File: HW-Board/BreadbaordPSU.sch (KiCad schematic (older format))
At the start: 12 parts

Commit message: sync
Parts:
- added C2, C4: 2.2u, symbol Device:C_Small
- added C3: 1u, symbol Device:C_Small
- added J2: Outputs, symbol Connector:Screw_Terminal_01x03
- added R2: 0r, symbol Device:R
- added U1: MAX6241, Housings_SOIC:SOIC-8_3.9x4.9mm_Pitch1.27mm, symbol Peters:MAX6241
- gave numbers to parts that had none: 12
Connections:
- net labels added: +4.096Vref, GNDA
- wire segments 25 -> 49
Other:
- note added: "Banana binding posts"
- note added: "Mind noise in layout"

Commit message: sync
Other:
- note added: "Todo:\n\nMerge to fewer opamps\nex. OPA2189IDR"
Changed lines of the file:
@@
 Text Notes 8500 5100 0    50   ~ 0
 Banana binding posts
+Text Notes 1400 6500 0    50   ~ 0
+Todo:\n\nMerge to fewer opamps\nex. OPA2189IDR
 $EndSCHEMATC

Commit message: SYNC
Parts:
- D1: value D_Zener -> 10V
- Q1: symbol Peters:Si4435 -> BreadbaordPSU-rescue:Si4435-Peters
- R1: value R -> 100k
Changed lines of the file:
@@
 	4150 1550 4250 1550
 $Comp
-L Peters:Si4435 Q1
+L BreadbaordPSU-rescue:Si4435-Peters Q1
 U 1 1 5CF021A1
 P 2300 1350
@@
 P 2650 1400
 F 0 "D1" V 2604 1479 50  0000 L CNN
-F 1 "D_Zener" V 2695 1479 50  0000 L CNN
+F 1 "10V" V 2695 1479 50  0000 L CNN
 F 2 "" H 2650 1400 50  0001 C CNN
 F 3 "~" H 2650 1400 50  0001 C CNN
@@
 P 2300 1700
 F 0 "R1" H 2370 1746 50  0000 L CNN
-F 1 "R" H 2370 1655 50  0000 L CNN
+F 1 "100k" H 2370 1655 50  0000 L CNN
 F 2 "" V 2230 1700 50  0001 C CNN
 F 3 "~" H 2300 1700 50  0001 C CNN

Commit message: sync
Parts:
- C1: value CP -> 100u
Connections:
- net at D1.1 (K), F1.1, Q1.1 (S): no longer Q1.2 (S), Q1.3 (S)
- net at C1.1, J1.2 (Pin_2), Q1.5 (D): no longer Q1.6 (D), Q1.7 (D), Q1.8 (D)
- new net: Q1.2 (S), Q1.3 (S)
- new net: Q1.6 (D), Q1.7 (D), Q1.8 (D)
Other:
- note added: "Max 15V"
- moved on the sheet: C1, D1, J1, Q1, R1
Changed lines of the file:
@@
 L Connector:Screw_Terminal_01x02 J1
 U 1 1 5CF83871
-P 1450 1350
-F 0 "J1" H 1368 1025 50  0000 C CNN
-F 1 "vin" H 1368 1116 50  0000 C CNN
-F 2 "" H 1450 1350 50  0001 C CNN
-F 3 "~" H 1450 1350 50  0001 C CNN
-	1    1450 1350
+P 1100 1350
+F 0 "J1" H 1018 1025 50  0000 C CNN
+F 1 "vin" H 1018 1116 50  0000 C CNN
+F 2 "" H 1100 1350 50  0001 C CNN
+F 3 "~" H 1100 1350 50  0001 C CNN
+	1    1100 1350
 	-1   0    0    1
 $EndComp
@@
 L power:GNDPWR #PWR0105
 U 1 1 5CF84A70
-P 1650 1400
-F 0 "#PWR0105" H 1650 1200 50  0001 C CNN
-F 1 "GNDPWR" H 1654 1246 50  0000 C CNN
-F 2 "" H 1650 1350 50  0001 C CNN
-F 3 "" H 1650 1350 50  0001 C CNN
-	1    1650 1400
-	1    0    0    -1
-$EndComp
-Wire Wire Line
-	1650 1350 1650 1400
+P 1300 1400
+F 0 "#PWR0105" H 1300 1200 50  0001 C CNN
+F 1 "GNDPWR" H 1304 1246 50  0000 C CNN
+F 2 "" H 1300 1350 50  0001 C CNN
+F 3 "" H 1300 1350 50  0001 C CNN
+	1    1300 1400
+	1    0    0    -1
+$EndComp
+Wire Wire Line
+	1300 1350 1300 1400
 $Comp
 L power:+12V #PWR0106
@@
 L BreadbaordPSU-rescue:Si4435-Peters Q1
 U 1 1 5CF021A1
-P 2300 1350
-F 0 "Q1" V 2643 1350 50  0000 C CNN
-F 1 "Si4435" V 2552 1350 50  0000 C CNN
-F 2 "Package_SO:SOIC-8_3.9x4.9mm_P1.27mm" H 2050 1650 50  0001 C CNN
-F 3 "https://www.vishay.com/docs/72123/72123.pdf" H 2150 1750 50  0001 C CNN
-	1    2300 1350
+P 1950 1350
+F 0 "Q1" V 2293 1350 50  0000 C CNN
+F 1 "Si4435" V 2202 1350 50  0000 C CNN
+F 2 "Package_SO:SOIC-8_3.9x4.9mm_P1.27mm" H 1700 1650 50  0001 C CNN
+F 3 "https://www.vishay.com/docs/72123/72123.pdf" H 1800 1750 50  0001 C CNN
+	1    1950 1350
 	0    -1   -1   0
 $EndComp
@@
 L Device:D_Zener D1
 U 1 1 5CF032D9
-P 2650 1400
-F 0 "D1" V 2604 1479 50  0000 L CNN
-F 1 "10V" V 2695 1479 50  0000 L CNN
-F 2 "" H 2650 1400 50  0001 C CNN
-F 3 "~" H 2650 1400 50  0001 C CNN
-	1    2650 1400
+P 2300 1400
+F 0 "D1" V 2254 1479 50  0000 L CNN
+F 1 "10V" V 2345 1479 50  0000 L CNN
+F 2 "" H 2300 1400 50  0001 C CNN
+F 3 "~" H 2300 1400 50  0001 C CNN
+	1    2300 1400
 	0    1    1    0
 $EndComp
@@
 L Device:R R1
 U 1 1 5CF126E3
-P 2300 1700
-F 0 "R1" H 2370 1746 50  0000 L CNN
-F 1 "100k" H 2370 1655 50  0000 L CNN
-F 2 "" V 2230 1700 50  0001 C CNN
-F 3 "~" H 2300 1700 50  0001 C CNN
-	1    2300 1700
-	1    0    0    -1
-$EndComp
-Wire Wire Line
-	2300 1450 2300 1550
-Wire Wire Line
-	2450 1250 2500 1250
-Connection ~ 2500 1250
-Wire Wire Line
-	2500 1250 2650 1250
-Wire Wire Line
-	2650 1550 2300 1550
-Connection ~ 2300 1550
+P 1950 1700
+F 0 "R1" H 2020 1746 50  0000 L CNN
+F 1 "100k" H 2020 1655 50  0000 L CNN
+F 2 "" V 1880 1700 50  0001 C CNN
+F 3 "~" H 1950 1700 50  0001 C CNN
+	1    1950 1700
+	1    0    0    -1
+$EndComp
+Wire Wire Line
+	1950 1450 1950 1550
+Wire Wire Line
+	2300 1550 1950 1550
+Connection ~ 1950 1550
 $Comp
 L power:GNDPWR #PWR0108
 U 1 1 5CF32200
-P 2300 1900
-F 0 "#PWR0108" H 2300 1700 50  0001 C CNN
-F 1 "GNDPWR" H 2304 1746 50  0000 C CNN
-F 2 "" H 2300 1850 50  0001 C CNN
-F 3 "" H 2300 1850 50  0001 C CNN
-	1    2300 1900
-	1    0    0    -1
-$EndComp
-Wire Wire Line
-	2300 1850 2300 1900
-Wire Wire Line
-	2150 1250 2100 1250
-Connection ~ 2100 1250
-Wire Wire Line
-	2100 1250 2000 1250
+P 1950 1900
+F 0 "#PWR0108" H 1950 1700 50  0001 C CNN
+F 1 "GNDPWR" H 1954 1746 50  0000 C CNN
+F 2 "" H 1950 1850 50  0001 C CNN
+F 3 "" H 1950 1850 50  0001 C CNN
+	1    1950 1900
+	1    0    0    -1
+$EndComp
+Wire Wire Line
+	1950 1850 1950 1900
 $Comp
 L Device:CP C1
 U 1 1 5CF42D89
-P 2000 1400
-F 0 "C1" H 2118 1446 50  0000 L CNN
-F 1 "CP" H 2118 1355 50  0000 L CNN
-F 2 "" H 2038 1250 50  0001 C CNN
-F 3 "~" H 2000 1400 50  0001 C CNN
-	1    2000 1400
+P 1650 1400
+F 0 "C1" H 1500 1300 50  0000 L CNN
+F 1 "100u" H 1650 1300 50  0000 L CNN
+F 2 "" H 1688 1250 50  0001 C CNN
+F 3 "~" H 1650 1400 50  0001 C CNN
+	1    1650 1400
 	1    0    0    -1
 $EndComp
@@
 L power:GNDPWR #PWR0109
 U 1 1 5CF437BA
-P 2000 1900
-F 0 "#PWR0109" H 2000 1700 50  0001 C CNN
-F 1 "GNDPWR" H 2004 1746 50  0000 C CNN
-F 2 "" H 2000 1850 50  0001 C CNN
-F 3 "" H 2000 1850 50  0001 C CNN
-	1    2000 1900
-	1    0    0    -1
-$EndComp
-Wire Wire Line
-	2000 1550 2000 1900
-Wire Wire Line
-	1650 1250 2000 1250
-Connection ~ 2000 1250
+P 1650 1900
+F 0 "#PWR0109" H 1650 1700 50  0001 C CNN
+F 1 "GNDPWR" H 1654 1746 50  0000 C CNN
+F 2 "" H 1650 1850 50  0001 C CNN
+F 3 "" H 1650 1850 50  0001 C CNN
+	1    1650 1900
+	1    0    0    -1
+$EndComp
+Wire Wire Line
+	1650 1550 1650 1900
+Wire Wire Line
+	1300 1250 1650 1250
+Connection ~ 1650 1250
 Wire Wire Line
 	3150 1250 3300 1250
-Wire Wire Line
-	2850 1250 2650 1250
-Connection ~ 2650 1250
+Connection ~ 2300 1250
 $Comp
 L Mechanical:MountingHole H1
@@
 	1    0    0    -1
 $EndComp
-Text Notes 900  1800 0    50   ~ 0
+Text Notes 550  1800 0    50   ~ 0
 Banana binding posts
 Text Notes 8500 5100 0    50   ~ 0
@@
 Text Notes 1400 6500 0    50   ~ 0
 Todo:\n\nMerge to fewer opamps\nex. OPA2189IDR
+Text Notes 650  1300 0    50   ~ 0
+Max 15V
+Wire Wire Line
+	1650 1250 1800 1250
+Wire Wire Line
+	2100 1250 2300 1250
+Wire Wire Line
+	2300 1250 2850 1250
 $EndSCHEMATC

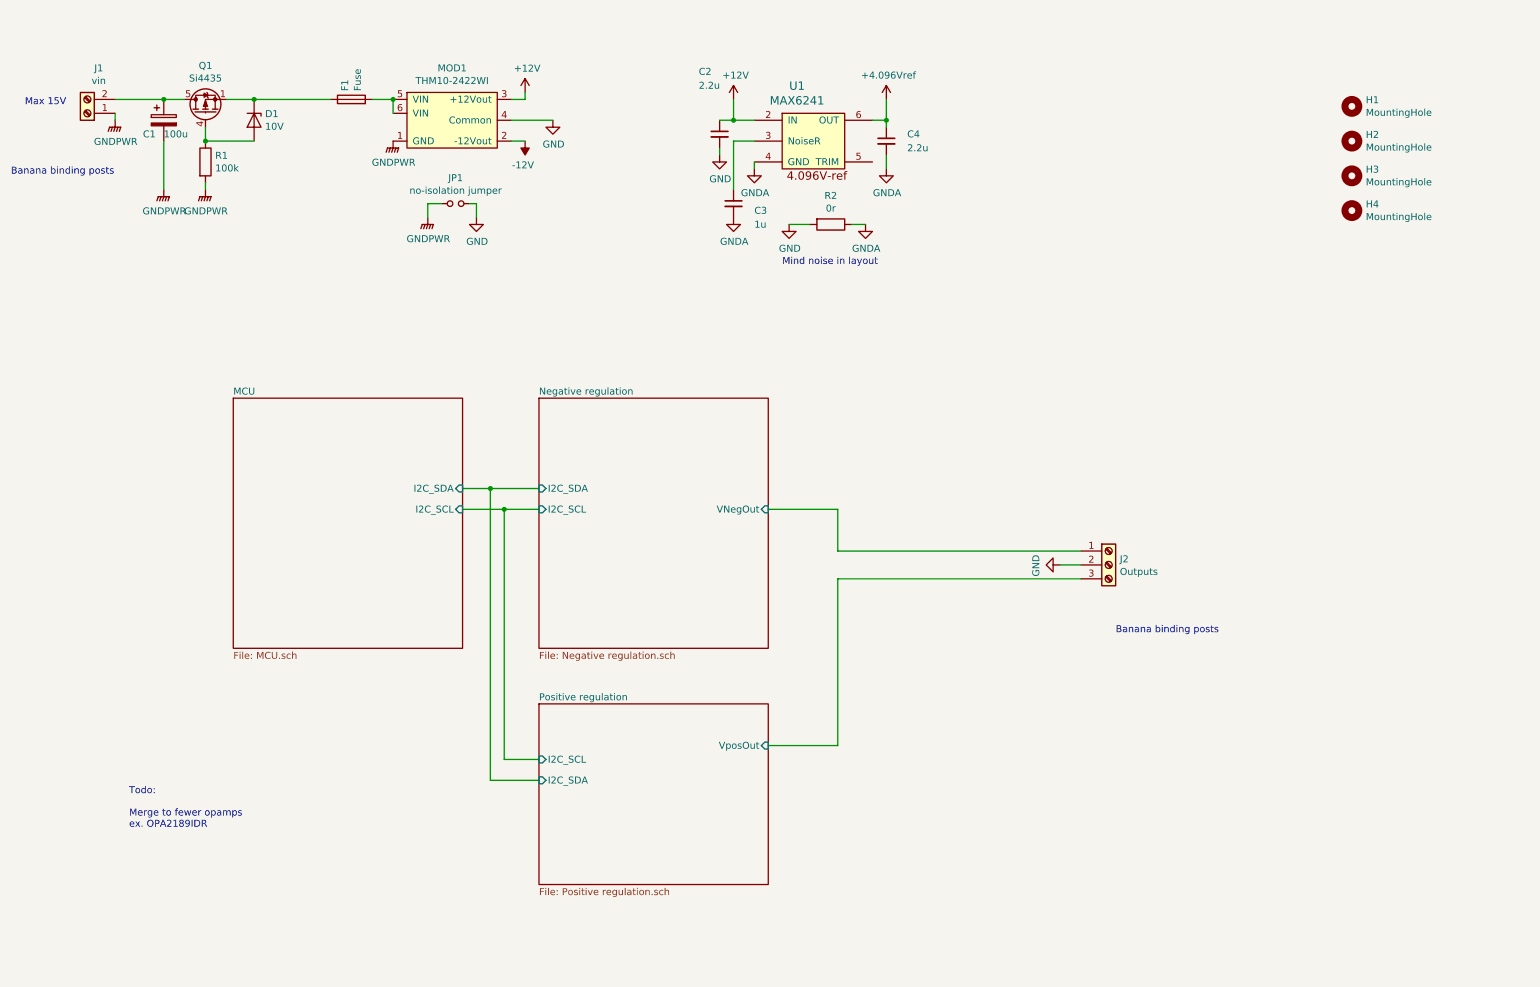
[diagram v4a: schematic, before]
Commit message: 5v isolation and better opamps
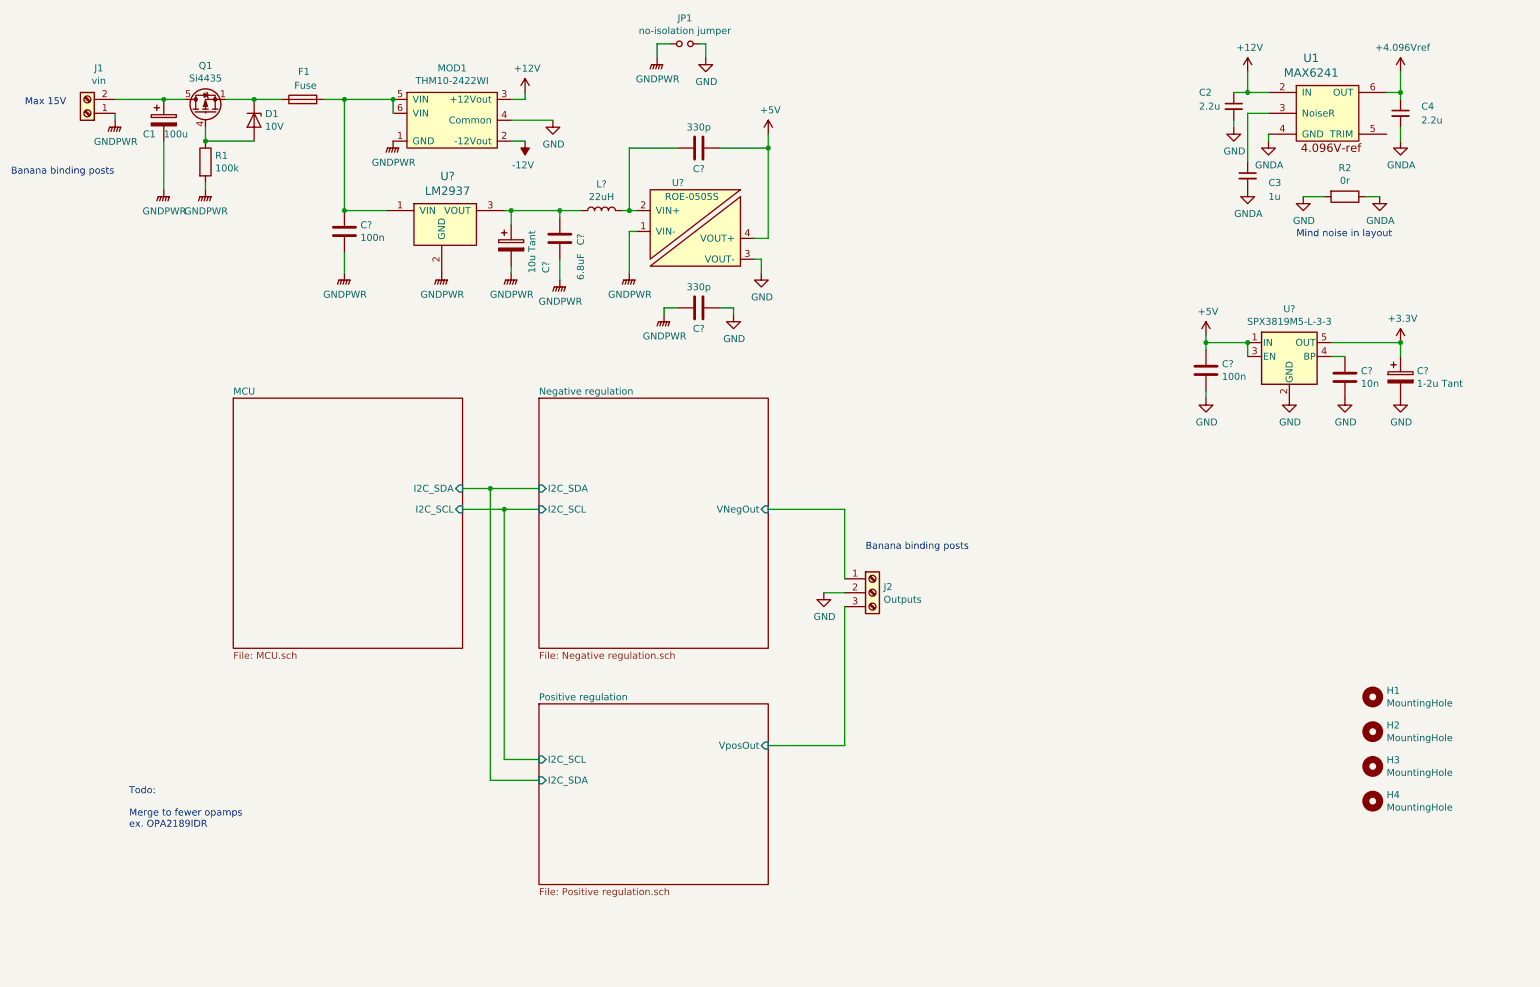
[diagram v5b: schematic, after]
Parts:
- added C?: 10n, symbol Device:C
- added C?: 1-2u Tant, symbol Device:CP
- added C? (x2): 100n, symbol Device:C
- added C?: 10u Tant, symbol Device:CP
- added C?: 6.8uF, symbol Device:C
- added C? (x2): 330p, symbol Device:C
- added L?: 22uH, symbol Device:L
- added U?: SPX3819M5-L-3-3, Package_TO_SOT_SMD:SOT-23-5, symbol Regulator_Linear:SPX3819M5-L-3-3
- added U?: LM2937, TO_SOT_Packages_SMD:SOT-223-3_TabPin2, symbol Peters:LM2937
- added U?: ROE-0505S, symbol Peters:ROE-0505S
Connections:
- net +3V3: now also C?.1, U?.5 (OUT)
- net GND: now also C?.1, C?.2, C?.2, C?.2, U?.2 (GND), U?.3 (VOUT-)
- net GNDPWR: now also C?.2, C?.2, C?.2, C?.2, U?.1 (VIN-), U?.2 (GND)
- net at F1.2, MOD1.5 (VIN), MOD1.6 (VIN): now also C?.1, U?.1 (VIN)
- new net: C?.1, U?.4 (BP)
- new net: C?.1, C?.1, L?.1, U?.3 (VOUT)
- new net: C?.2, L?.2, U?.2 (VIN+)
- new net +5V: C?.1, C?.1, U?.1 (IN), U?.3 (EN), U?.4 (VOUT+)
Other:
- moved on the sheet: C2, C3, C4, F1, H1, H2, H3, H4, J2, JP1, R2, U1

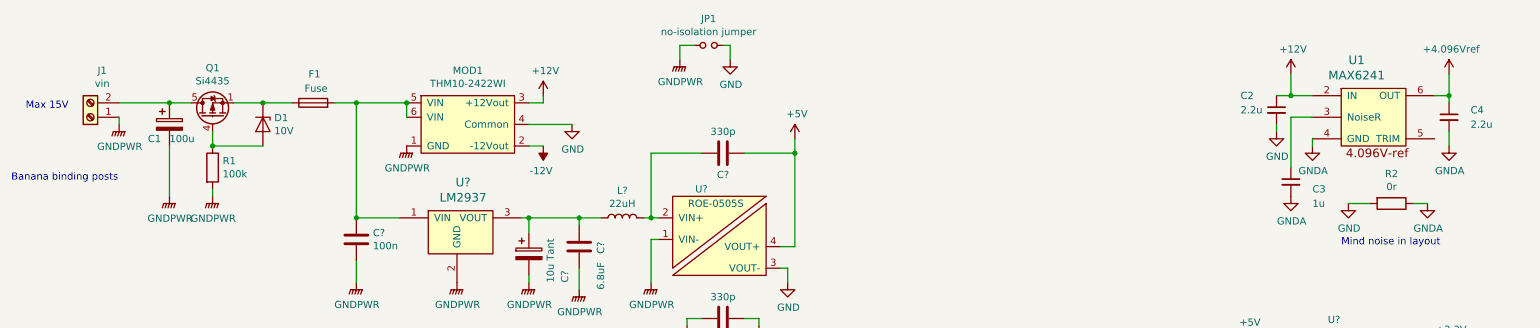
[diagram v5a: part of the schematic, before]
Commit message: added schmidt on encoder button
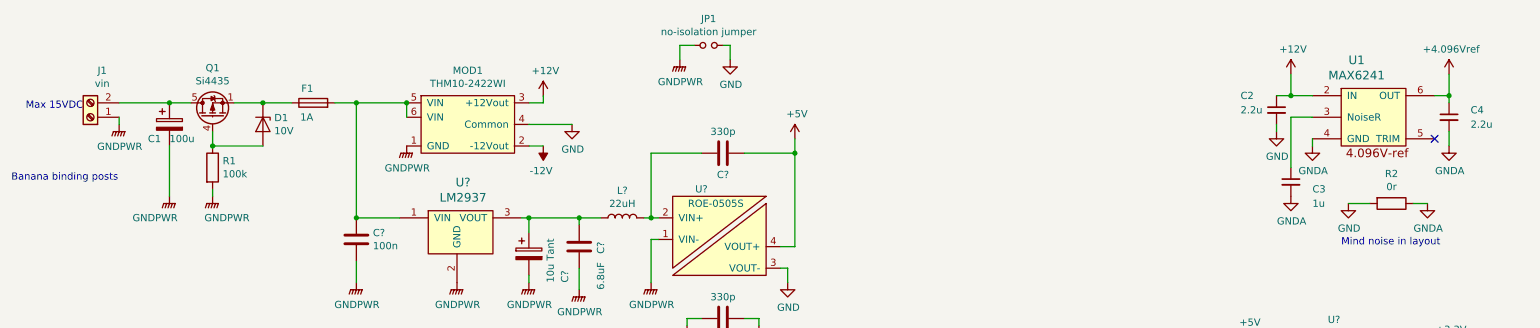
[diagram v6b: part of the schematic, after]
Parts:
- F1: value Fuse -> 1A
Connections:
- no-connect marks 0 -> 1
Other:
- note added: "Max 15VDC"
- note removed: "Max 15V"
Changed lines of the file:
@@
 U 1 1 5CEEEF1E
 P 2650 1250
-F 0 "F1" V 2850 1200 50  0000 L CNN
-F 1 "Fuse" V 2750 1150 50  0000 L CNN
+F 0 "F1" V 2750 1250 50  0000 L CNN
+F 1 "1A" V 2550 1250 50  0000 L CNN
 F 2 "" V 2580 1250 50  0001 C CNN
 F 3 "~" H 2650 1250 50  0001 C CNN
@@
 P 1950 1900
 F 0 "#PWR0108" H 1950 1700 50  0001 C CNN
-F 1 "GNDPWR" H 1954 1746 50  0000 C CNN
+F 1 "GNDPWR" H 2050 1750 50  0000 C CNN
 F 2 "" H 1950 1850 50  0001 C CNN
 F 3 "" H 1950 1850 50  0001 C CNN
@@
 P 1650 1900
 F 0 "#PWR0109" H 1650 1700 50  0001 C CNN
-F 1 "GNDPWR" H 1654 1746 50  0000 C CNN
+F 1 "GNDPWR" H 1550 1750 50  0000 C CNN
 F 2 "" H 1650 1850 50  0001 C CNN
 F 3 "" H 1650 1850 50  0001 C CNN
@@
 Todo:\n\nMerge to fewer opamps\nex. OPA2189IDR
 Text Notes 650  1300 0    50   ~ 0
-Max 15V
+Max 15VDC
 Wire Wire Line
 	1650 1250 1800 1250
@@
 Wire Wire Line
 	9150 3400 9150 3350
+NoConn ~ 10450 1500
 $EndSCHEMATC
